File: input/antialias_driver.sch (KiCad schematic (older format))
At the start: 23 parts, among them U104 THS4131

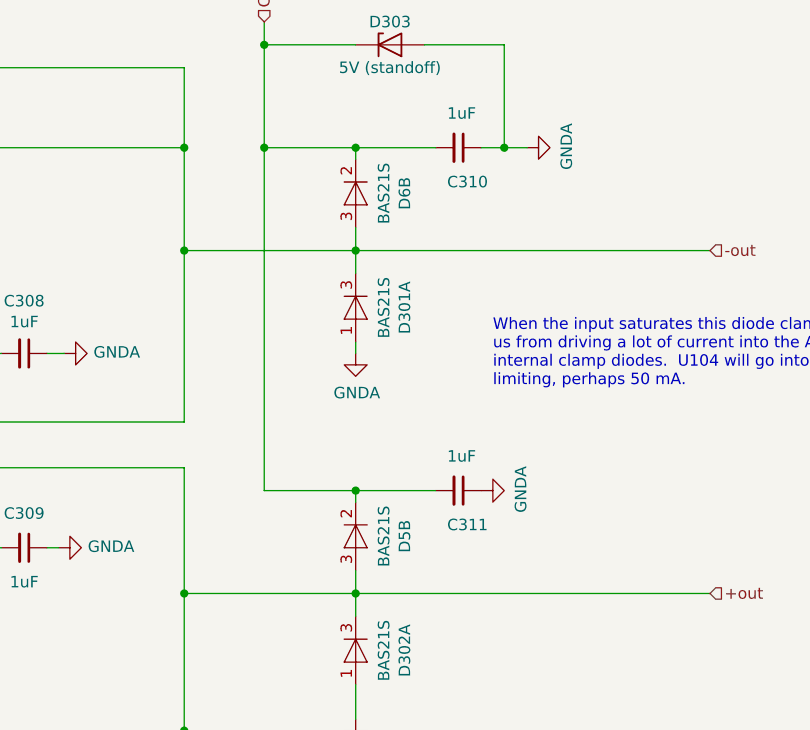
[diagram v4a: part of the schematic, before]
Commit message: Input board is nearly ready to send off for the first spin.
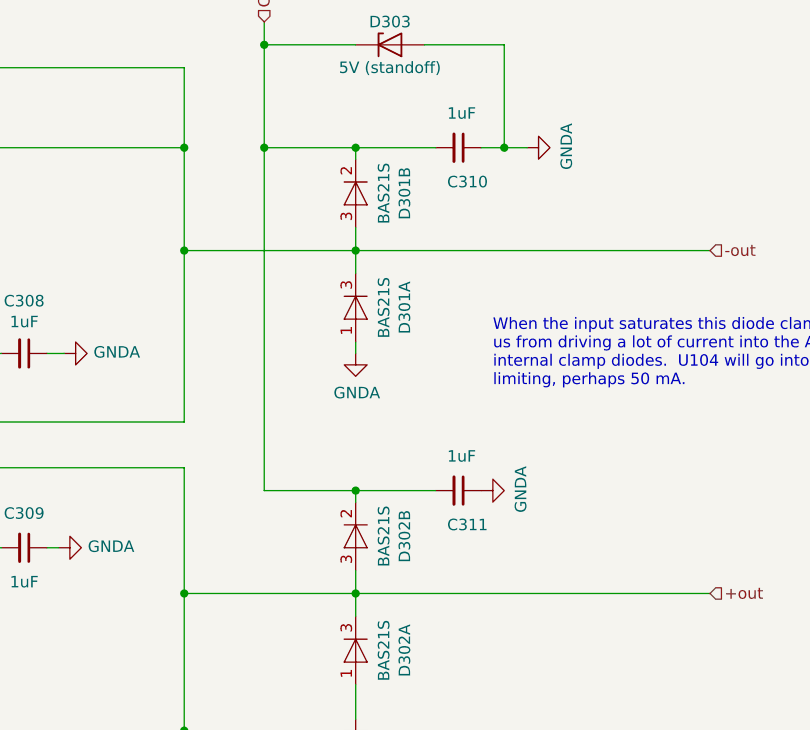
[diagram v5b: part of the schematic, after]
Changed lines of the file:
@@
 $Descr A4 11693 8268
 encoding utf-8
-Sheet 3 21
+Sheet 18 21
 Title ""
 Date ""
@@
 AR Path="/5DFCF14D/5DE42731/5E3F98E8" Ref="D?"  Part="2"
 AR Path="/5DFCF14D/5DE6CDF8/5E3F98E8" Ref="D109"  Part="1"
-AR Path="/5E448095/5DE6CDF8/5E3F98E8" Ref="D1"  Part="1"
+AR Path="/5E448095/5DE6CDF8/5E3F98E8" Ref="D211"  Part="1"
 AR Path="/5E45936E/5DE6CDF8/5E3F98E8" Ref="D301"  Part="1"
 F 0 "D301" H 7000 3115 50  0000 C CNN
@@
 AR Path="/5DFCF14D/5DE42731/5E3F98EE" Ref="D?"  Part="1"
 AR Path="/5DFCF14D/5DE6CDF8/5E3F98EE" Ref="D109"  Part="2"
-AR Path="/5E448095/5DE6CDF8/5E3F98EE" Ref="D105"  Part="2"
-AR Path="/5E45936E/5DE6CDF8/5E3F98EE" Ref="D6"  Part="2"
-F 0 "D6" H 7000 2615 50  0000 C CNN
+AR Path="/5E448095/5DE6CDF8/5E3F98EE" Ref="D211"  Part="2"
+AR Path="/5E45936E/5DE6CDF8/5E3F98EE" Ref="D301"  Part="2"
+F 0 "D301" H 7000 2615 50  0000 C CNN
 F 1 "BAS21S" H 7000 2524 50  0000 C CNN
 F 2 "Package_TO_SOT_SMD:SOT-23" H 7000 2250 50  0001 C CNN
@@
 AR Path="/5DFCF14D/5DE42731/5E403D66" Ref="D?"  Part="1"
 AR Path="/5DFCF14D/5DE6CDF8/5E403D66" Ref="D110"  Part="2"
-AR Path="/5E448095/5DE6CDF8/5E403D66" Ref="D108"  Part="2"
-AR Path="/5E45936E/5DE6CDF8/5E403D66" Ref="D5"  Part="2"
-F 0 "D5" H 7000 4115 50  0000 C CNN
+AR Path="/5E448095/5DE6CDF8/5E403D66" Ref="D201"  Part="2"
+AR Path="/5E45936E/5DE6CDF8/5E403D66" Ref="D302"  Part="2"
+F 0 "D302" H 7000 4115 50  0000 C CNN
 F 1 "BAS21S" H 7000 4024 50  0000 C CNN
 F 2 "Package_TO_SOT_SMD:SOT-23" H 7000 3750 50  0001 C CNN

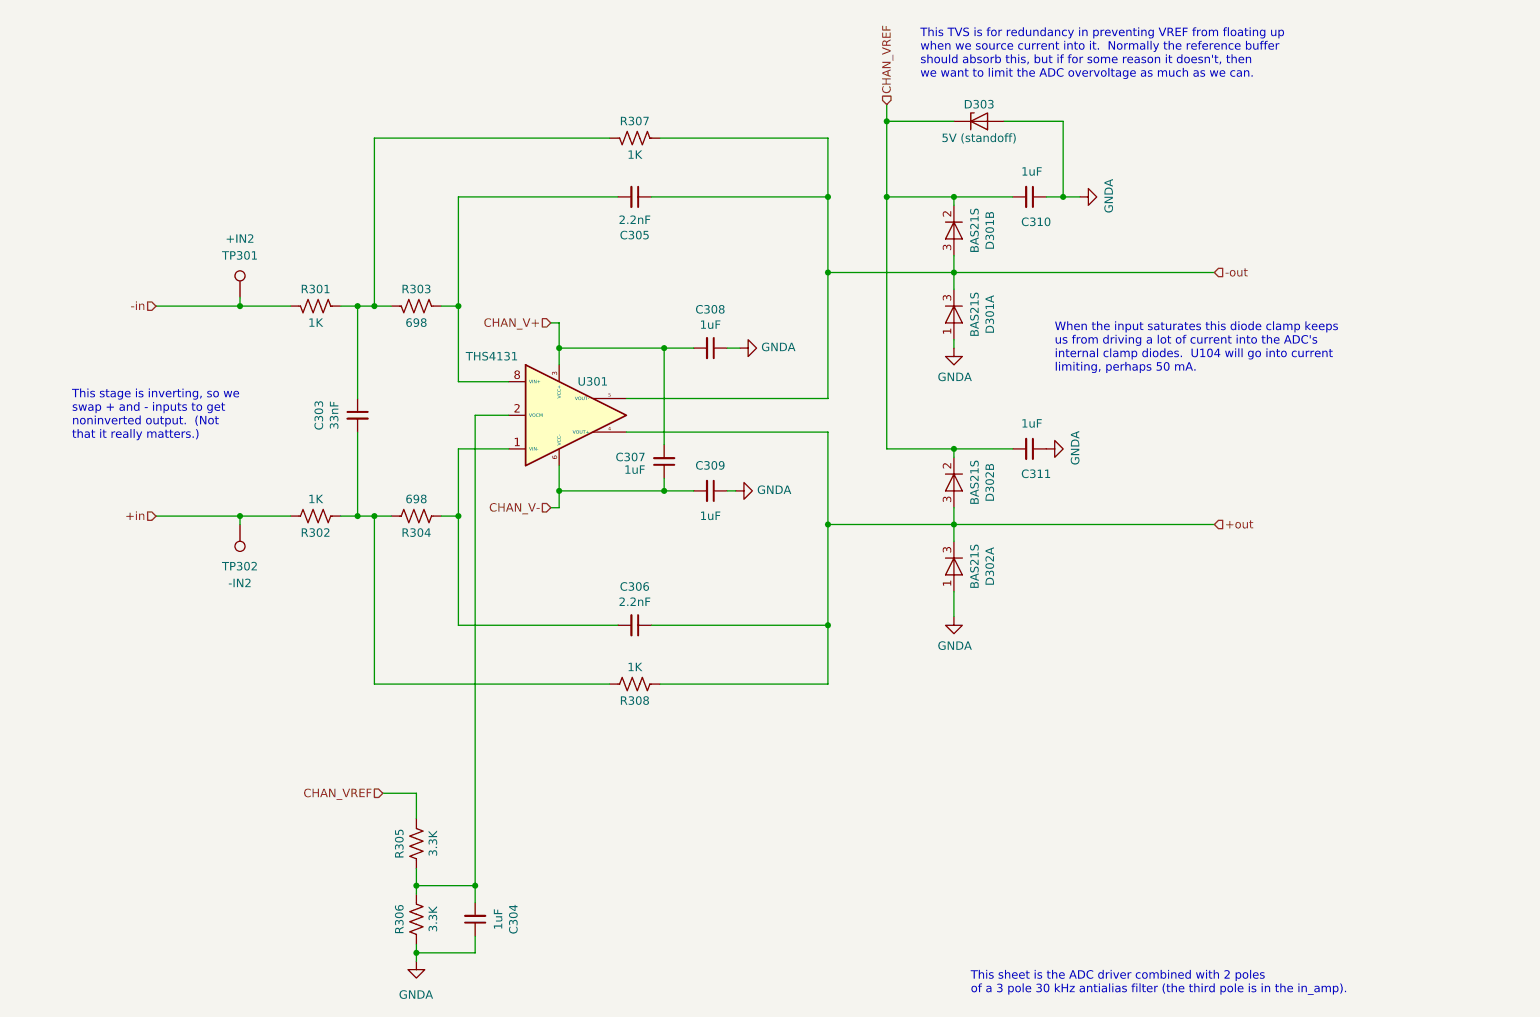
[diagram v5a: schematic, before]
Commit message: Various tweaks to schematic which help in the PCB view, mainly getting informative net names. Also unscrambled the + and - paths in the input channel.  This avoided a cross-over before the first stage, and an unintended inversion, but mostly just made net naming less confusing.
Getting better net names made it easier to review the PCB to see if it made sense.  I checked
the ICs on the PCB against the datasheet pinout, and while doing this fixed an actual bug where
I had BIST-+ and BIST+-swapped.

I made some tweaks on the PCB to try to equalize the copper area on the input nets so as to
match the capacitance.  I tweaked the top-side ground pours somewhat, adding in the regulator
area, removing around the high speed traces.

Some changes from gerber viewing.  I reduced the solder mask clearances so that we get mask
web between the SOIC and DFN pads.  I reduced the pad size of the big via from 1.2 to 1.0 mm.
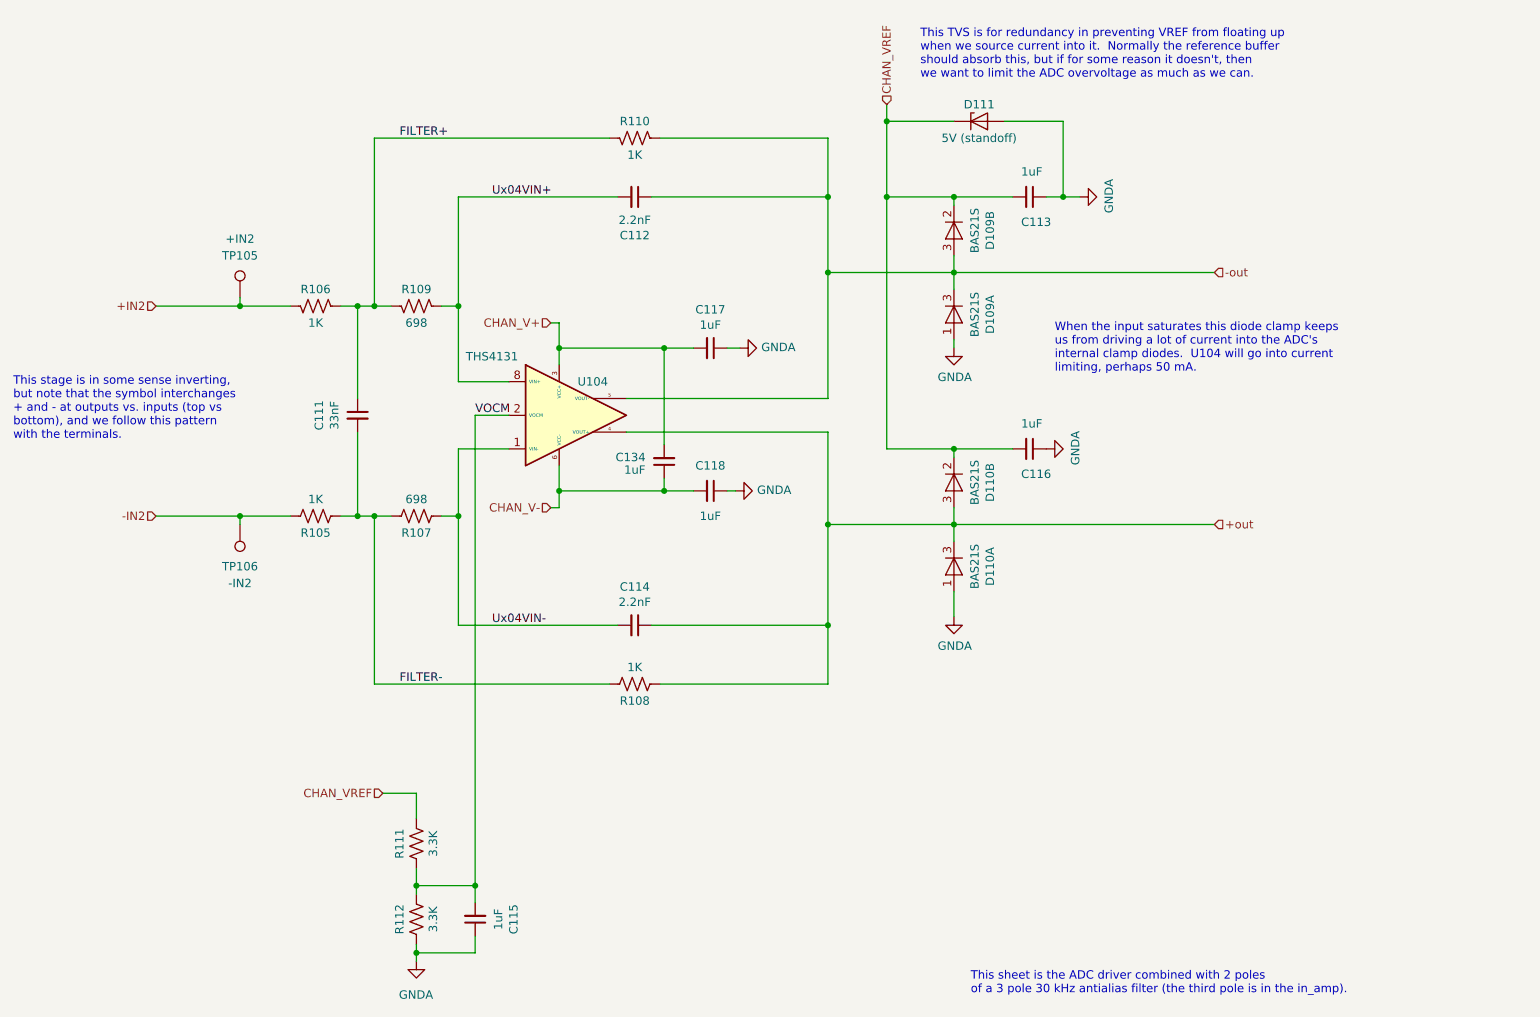
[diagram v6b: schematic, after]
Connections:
- net Ux04VIN-: now reaches C114.2, R107.1, U104.1 (VIN-)
- net FILTER-: now reaches C111.2, R105.1, R107.2, R108.2
- net FILTER+: now reaches C111.1, R106.1, R109.2, R110.2
- net VOCM: now reaches C115.2, R111.1, R112.2, U104.2 (VOCM)
- net Ux04VIN+: now reaches C112.2, R109.1, U104.8 (VIN+)
- net +in renamed -IN2
- net -in renamed +IN2
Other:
- note added: "This stage is in some sense inverting,\nbut note that the symbol interchanges\n+ and - at outputs vs. inputs (top vs\nbottom), and we follow this pattern \nwith the terminals."
- note removed: "This stage is inverting, so we \nswap + and - inputs to get\nnoninverted output. (Not \nthat it really matters.)"

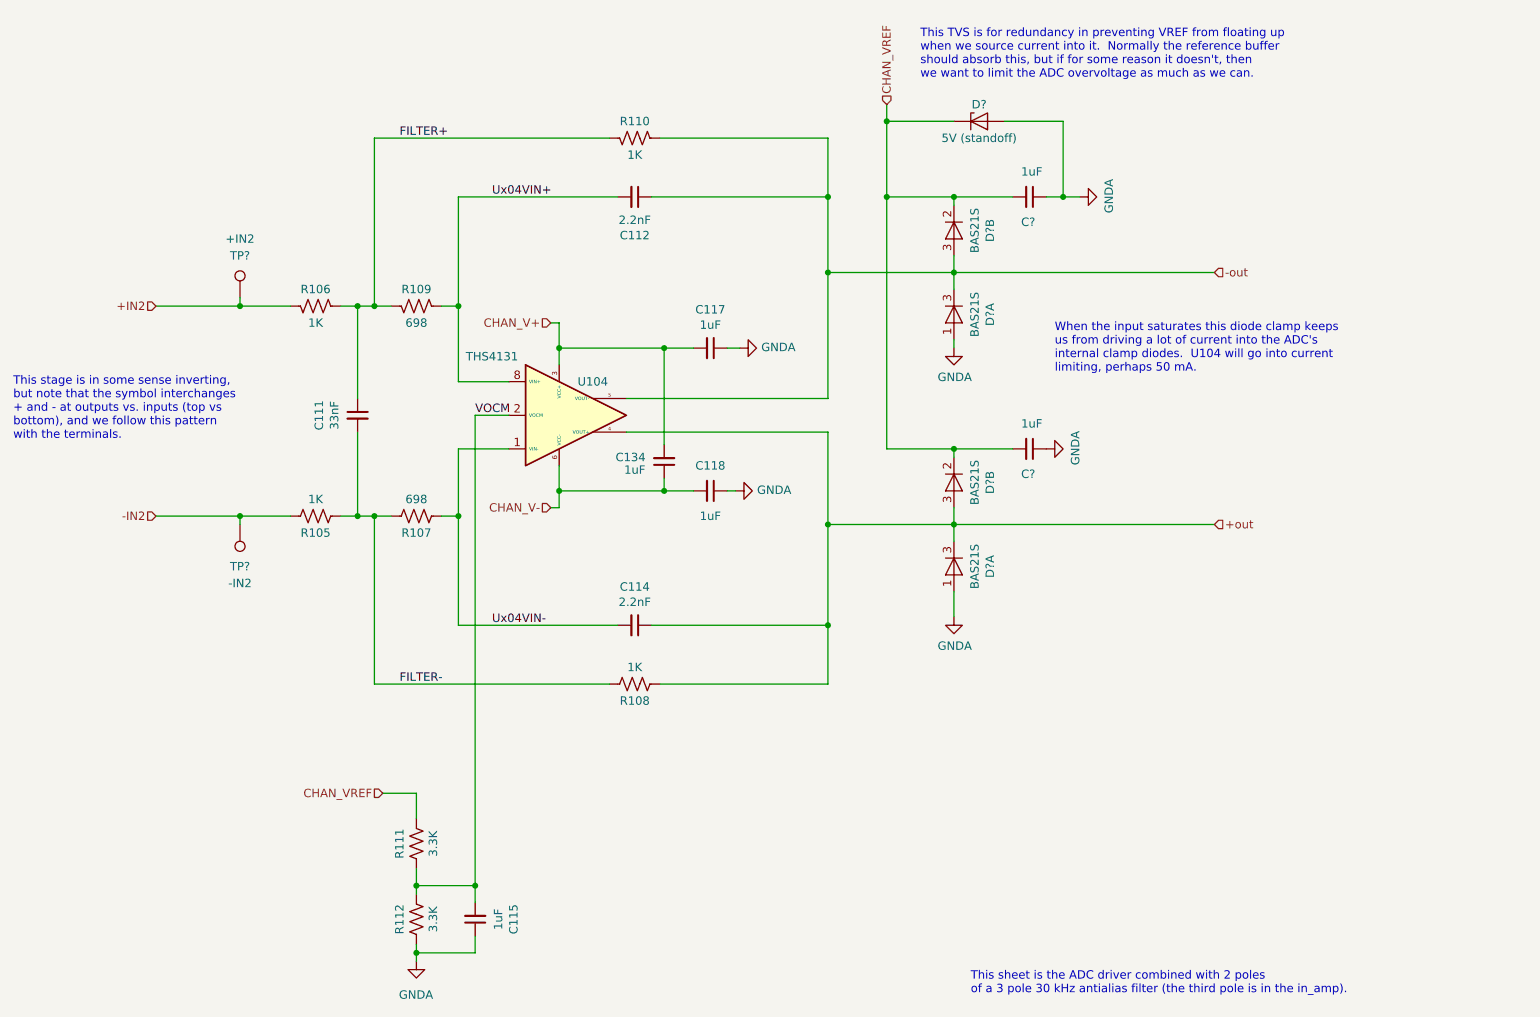
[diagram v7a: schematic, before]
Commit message: Checkpoint of state before I start schematic revisions for the next version of the input board. There are not any substantive modifications to the input board, but some broad changes in component attributes related enabling a fabrication quote.
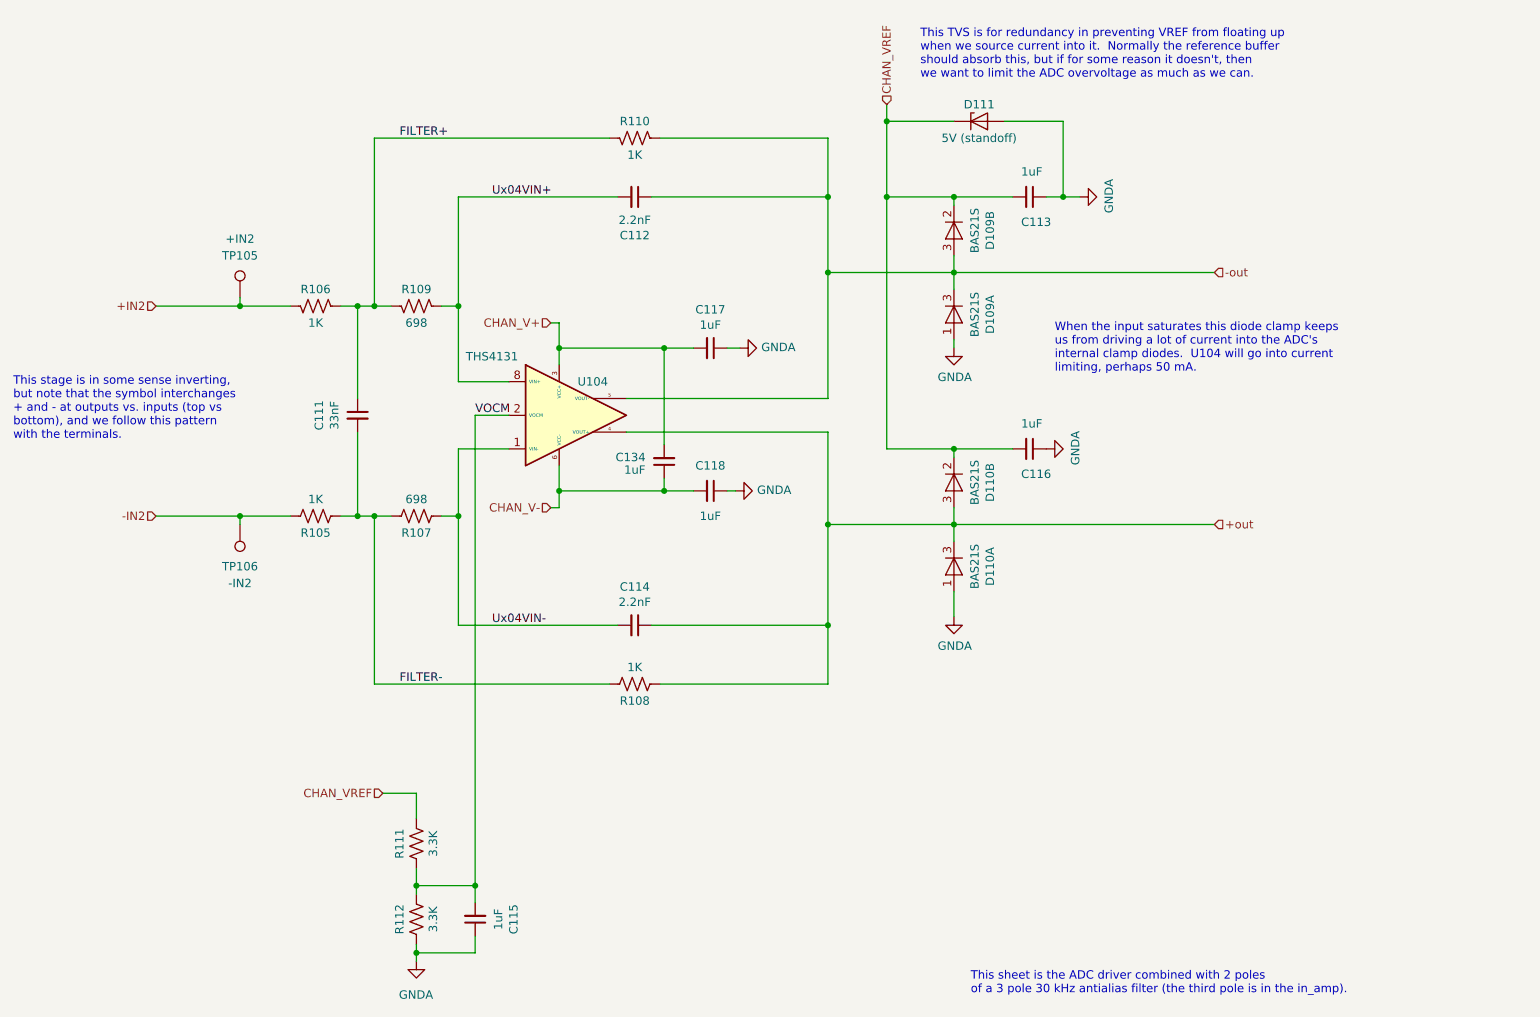
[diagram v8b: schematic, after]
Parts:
- C111: MPN (none) -> CGA4J2C0G1H333J125AA; Manufacturer (none) -> TDK Corporation
- C112, C114: MPN (none) -> GRM1885C1H222GA01D; Manufacturer (none) -> Murata Electronics
- C113, C115, C116, C117, C118, C134: Manufacturer (none) -> Samsung Electro-Mechanics
- D109, D110: Manufacturer (none) -> ON Semiconductor
- D111: Manufacturer (none) -> Würth Elektronik
- R105, R106, R108, R110: MPN (none) -> ERA-3AEB102V; Manufacturer (none) -> Panasonic Electronic Components
- R107, R109: MPN (none) -> RT0603DRE07698RL; Manufacturer (none) -> Yageo
- R111, R112: MPN (none) -> RT0603FRE073K3L; Manufacturer (none) -> Yageo
- TP105, TP106: Description (none) -> Do Not Populate; MPN (none) -> DNP
- U104: MPN (none) -> THS4131CDR; Manufacturer (none) -> Texas Instruments
